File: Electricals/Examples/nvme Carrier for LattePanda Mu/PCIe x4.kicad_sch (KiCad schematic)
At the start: 24 parts, among them J200 Bus_PCI_Express_x4, J300 Bus_PCI_Express_x4, J81 Conn_01x03_Pin, J82 Conn_01x03_Pin

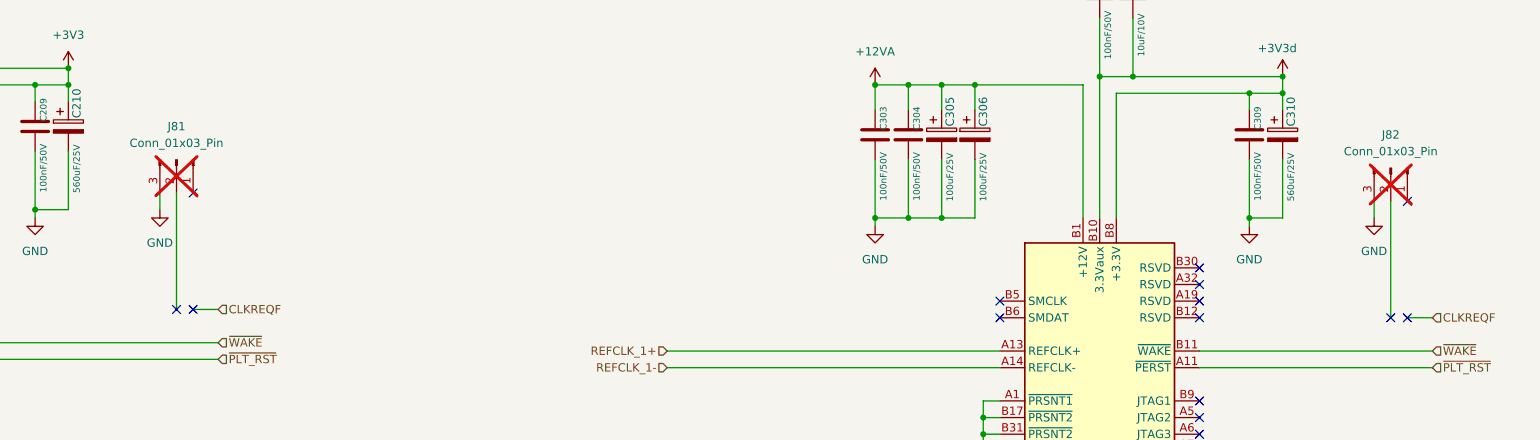
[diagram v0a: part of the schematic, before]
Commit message: Add BIOS Chip to Carrier
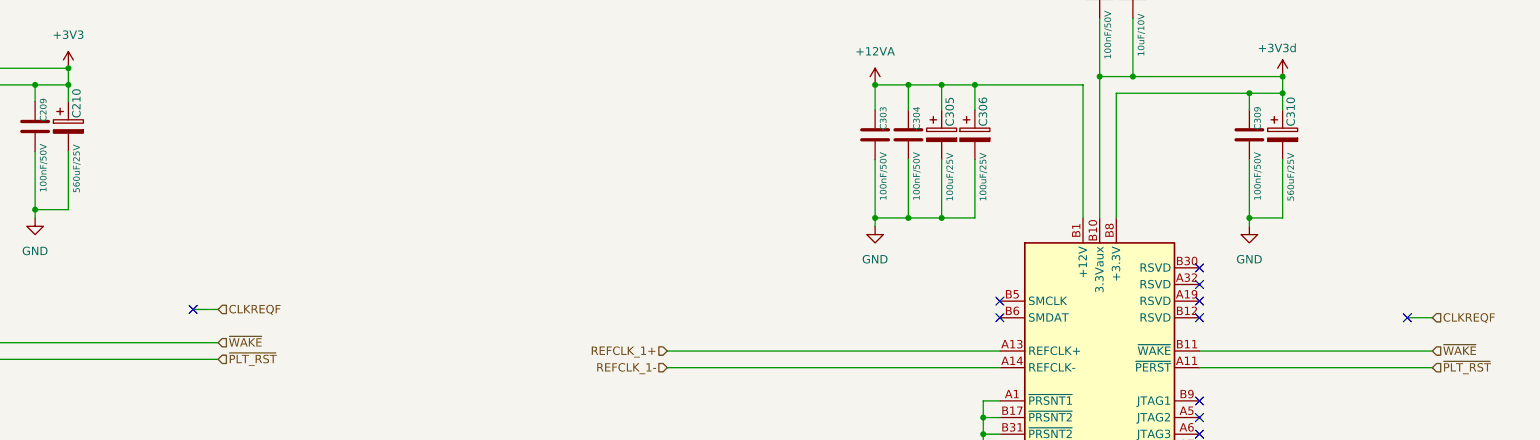
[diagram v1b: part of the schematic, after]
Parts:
- removed J81, J82: Conn_01x03_Pin, Connector_PinSocket_2.54mm:PinSocket_1x03_P2.54mm_Vertical, symbol Connector:Conn_01x03_Pin
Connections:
- no-connect marks 52 -> 48
